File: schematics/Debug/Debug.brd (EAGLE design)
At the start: 100 x 80 mm, 12 parts

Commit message: Debug plata
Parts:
- removed JP1: (no value), pinhead:1X06
- removed JP2, JP3, JP5, JP6, JP7, JP8: (no value), pinhead:1X02
- removed JP9: (no value), pinhead:1X03
- added BUS0, BUS1, RADIO_M1, RESET, U_ESP32, U_STM32: (no value), pinhead:1X02
- added GND: (no value), pinhead:1X06
- added SWD/UART: (no value), pinhead:1X03
- R1, R2: device resistor:0204/5 -> rcl:R0603
- moved S1 57.9 mm to (17.5, 16.2), turned to 270 degrees
- moved R1 51.9 mm to (6.08, 31.6), turned to 270 degrees
- moved R2 49.4 mm to (3.08, 31.6), turned to 270 degrees
- moved U$1 46.6 mm to (19.9, 39.2)
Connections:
- removed net N$1: JP5.2, U$1.TX1
- removed net N$10: JP1.1, JP1.2, JP1.3, JP1.4, JP1.5, JP1.6, JP3.1, JP6.2, JP8.1, JP9.3, S1.3, S1.4, U$1.GND0, U$1.GND1
- removed net N$11: JP9.2, U$1.SWDIO
- removed net N$12: JP9.1, U$1.SWDCLK
- removed net N$2: JP5.1, U$1.RX1
- removed net N$3: JP7.1, U$1.RX0
- removed net N$4: JP8.2, S1.1, S1.2, U$1.P$6
- removed net N$5: JP7.2, U$1.TX0
- removed net N$6: JP3.2, JP6.1, R2.2, U$1.VBUS0, U$1.VBUS1
- removed net N$9: JP2.2, U$1.M1
- new net BUS: BUS0.1, BUS1.2, R2.2, U$1.BUS0, U$1.BUS1
- new net GND: BUS0.2, BUS1.1, GND.1, GND.2, GND.3, GND.4, GND.5, GND.6, RESET.1, S1.3, S1.4, SWD/UART.3, U$1.GND0, U$1.GND1
- new net M1: RADIO_M1.2, U$1.M1
- new net RESET: RESET.2, S1.1, S1.2, U$1.RESET
- new net RX+: U$1.RX1, U_ESP32.1
- new net RX-: U$1.RX0, U_STM32.1
- new net SWC: SWD/UART.1, U$1.SWC
- new net SWD: SWD/UART.2, U$1.SWD
- new net TX+: U$1.TX1, U_ESP32.2
- new net TX-: U$1.TX0, U_STM32.2
- net N$7: now also RADIO_M1.1; no longer JP2.1
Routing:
- net GND: track 0.00 -> 117.0 mm
- net N$10: track 87.3 -> 0.00 mm
- net BUS: track 0.00 -> 83.8 mm, vias 0 -> 1
- net TX-: track 0.00 -> 40.7 mm, vias 0 -> 2
- net SWC: track 0.00 -> 36.8 mm
- net RX+: track 0.00 -> 34.6 mm
- net TX+: track 0.00 -> 33.8 mm
- net RX-: track 0.00 -> 33.6 mm, vias 0 -> 1
- net RESET: track 0.00 -> 30.9 mm, vias 0 -> 1
- net SWD: track 0.00 -> 29.6 mm
- net N$9: track 24.6 -> 0.00 mm
- net M1: track 0.00 -> 21.9 mm, vias 0 -> 1
- net N$12: track 21.1 -> 0.00 mm
- net N$4: track 13.7 -> 0.00 mm
- net N$6: track 12.8 -> 0.00 mm
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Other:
- board size 100 x 80 mm -> 37.1 x 39.3 mm
- board text added: "BUS"
- board text added: "GND"
- board text added: "RX"
- board text added: "SWC/TX"
- board text added: "SWD/RX"
- board text added: "TX"
- board text added: "Замкнуть для конфигурации радио"

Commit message: Очередная дебажная плата
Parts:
- removed BUS0, U_ESP32, U_STM32: (no value), pinhead:1X02
- removed GND: (no value), pinhead:1X06
- removed SWD/UART: (no value), pinhead:1X03
- added BUS2, BUS3, BUS4, DB_ESP, DB_STM, IO0, RESET1: (no value), pinhead:1X02
- added DL_ESP, DL_STM: (no value), pinhead:1X03
- added GND1: (no value), pinhead:1X06
- added S2, S3: (no value), switch-omron:B3F-10XX
- added U$2: USB-C, CanCubeSat:USB-C
- moved BUS1 37.8 mm to (33.9, 41.6), turned to 180 degrees
- moved RADIO_M1 19.5 mm to (24.0, 27.6), turned to 90 degrees
- moved R2 15.0 mm to (17.0, 26.0), turned to 0 degrees
- moved R1 11.2 mm to (17.0, 29.0), turned to 0 degrees
- moved RESET 10.5 mm to (20.9, 9.09), turned to 180 degrees
- moved U$1 5.81 mm to (20.0, 45.0)
- moved S1 3.91 mm to (20.9, 18.1), turned to 0 degrees
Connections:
- removed net RX+: U$1.RX1, U_ESP32.1
- removed net RX-: U$1.RX0, U_STM32.1
- removed net SWC: SWD/UART.1, U$1.SWC
- removed net SWD: SWD/UART.2, U$1.SWD
- removed net TX+: U$1.TX1, U_ESP32.2
- removed net TX-: U$1.TX0, U_STM32.2
- new net 3V3: BUS2.2, BUS3.2, U$1.SWC, U$2.SWC
- new net N$3: IO0.1, S3.3, S3.4, U$1.SWD
- new net RESET_STM: RESET1.2, S2.1, S2.2, U$2.RESET
- new net RX0: DB_ESP.1, U$1.RX0
- new net RX0_STM: DB_STM.1, U$2.RX0
- new net RX1: DL_ESP.2, U$1.RX1
- new net SWC_STM: DL_STM.3, U$2.TX1
- new net SWD_STM: DL_STM.2, U$2.RX1
- new net TX0: DB_ESP.2, U$1.TX0
- new net TX0_STM: DB_STM.2, U$2.TX0
- new net TX1: DL_ESP.3, U$1.TX1
- net BUS: now also BUS4.2, U$2.BUS0, U$2.BUS1; no longer BUS0.1
- net GND: now also BUS2.1, BUS3.1, BUS4.1, DL_STM.1, GND1.1, GND1.2, GND1.3, GND1.4, GND1.5, GND1.6, IO0.2, RESET1.1, S2.3, S2.4, S3.1, S3.2, U$2.GND0, U$2.GND1; no longer BUS0.2, GND.1, GND.2, GND.3, GND.4, GND.5, GND.6, SWD/UART.3
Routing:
- net GND: track 117.0 -> 187.2 mm, vias 0 -> 1
- net N$3: track 0.00 -> 49.2 mm, vias 0 -> 1
- net 3V3: track 0.00 -> 49.0 mm, vias 0 -> 1
- net BUS: track 83.8 -> 127.4 mm
- net TX-: track 40.7 -> 0.00 mm, vias 2 -> 0
- net RESET_STM: track 0.00 -> 37.1 mm, vias 0 -> 1
- net SWC: track 36.8 -> 0.00 mm
- net RX+: track 34.6 -> 0.00 mm
- net TX+: track 33.8 -> 0.00 mm
- net RX-: track 33.6 -> 0.00 mm, vias 1 -> 0
- net SWD: track 29.6 -> 0.00 mm
- net TX0: track 0.00 -> 29.5 mm, vias 0 -> 1
- net RX0: track 0.00 -> 24.5 mm
- net TX1: track 0.00 -> 17.0 mm
- net RX1: track 0.00 -> 16.4 mm
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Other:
- board size 37.1 x 39.3 mm -> 63.8 x 42.5 mm
- board text removed: "BUS"
- board text removed: "GND"
- board text removed: "RX"
- board text removed: "SWC/TX"
- board text removed: "SWD/RX"
- board text removed: "TX"

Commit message: Отладочная плата v2
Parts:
- removed BUS1, BUS2, BUS3, BUS4, DB_ESP, DB_STM, RADIO_M1, RESET, RESET1: (no value), pinhead:1X02
- removed DL_ESP, DL_STM: (no value), pinhead:1X03
- removed GND1: (no value), pinhead:1X06
- removed R1: 1k, rcl:R0603
- removed R2: 10k, rcl:R0603
- removed S1, S2, S3: (no value), switch-omron:B3F-10XX
- added C1, C2, C3: 1nF, rcl:C0603
- added DEBUG_STM32: (no value), pinhead:1X03
- added DOWNLOAD_ESP32: (no value), pinhead:1X05
- added DOWNLOAD_STM32, RADIO: (no value), pinhead:1X04
- added EN, NRST: (no value), switch-omron:B3F-10XX
- added ENABLE, GPIO0, JP1, JP5, JP6, JP7, JP8, NRESET: (no value), pinhead:1X02
- added JP2: (no value), pinhead:1X06
- IO0: device pinhead:1X02 -> switch-omron:B3F-10XX
- moved IO0 39.9 mm to (36.0, 49.0), turned to 90 degrees
- moved U$1 32.0 mm to (21.1, 77.0)
- moved U$2 32.0 mm to (55.1, 77.0)
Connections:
- removed net N$3: IO0.1, S3.3, S3.4, U$1.SWD
- removed net N$7: R1.2, RADIO_M1.1
- removed net N$8: R1.1, R2.1
- removed net RESET: RESET.2, S1.1, S1.2, U$1.RESET
- removed net RESET_STM: RESET1.2, S2.1, S2.2, U$2.RESET
- removed net RX0: DB_ESP.1, U$1.RX0
- removed net RX0_STM: DB_STM.1, U$2.RX0
- removed net SWC_STM: DL_STM.3, U$2.TX1
- removed net SWD_STM: DL_STM.2, U$2.RX1
- removed net TX0: DB_ESP.2, U$1.TX0
- removed net TX0_STM: DB_STM.2, U$2.TX0
- new net 3V3-S: JP1.1, U$1.NC/3V3
- new net EN: C2.2, DOWNLOAD_ESP32.5, EN.3, EN.4, ENABLE.2, U$1.NRST/EN
- new net IO0: C1.2, DOWNLOAD_ESP32.4, GPIO0.2, IO0.3, IO0.4, U$1.NC/GPIO
- new net NRST: C3.2, DOWNLOAD_STM32.4, NRESET.2, NRST.3, NRST.4, U$2.NRST/EN
- new net RX: DEBUG_STM32.3, U$2.RX0
- new net RXD: DOWNLOAD_ESP32.3, U$1.SWD/RXD
- new net SWC: DOWNLOAD_STM32.2, U$2.SWC/TXD
- new net SWD: DOWNLOAD_STM32.3, U$2.SWD/RXD
- new net TX: DEBUG_STM32.2, U$2.TX0
- new net TXD: DOWNLOAD_ESP32.2, U$1.SWC/TXD
- net 3V3: now also JP5.2, JP7.2, U$2.NC/3V3; no longer BUS2.2, BUS3.2, U$1.SWC, U$2.SWC
- net BUS: now also JP6.2, JP8.2, U$1.3V3/BUS0, U$1.3V3/BUS1, U$2.3V3/BUS0, U$2.3V3/BUS1; no longer BUS1.2, BUS4.2, R2.2, U$1.BUS0, U$1.BUS1, U$2.BUS0, U$2.BUS1
- net GND: now also C1.1, C2.1, C3.1, DEBUG_STM32.1, DOWNLOAD_ESP32.1, DOWNLOAD_STM32.1, EN.1, EN.2, ENABLE.1, GPIO0.1, IO0.1, JP2.1, JP2.2, JP2.3, JP2.4, JP2.5, JP2.6, JP5.1, JP6.1, JP7.1, JP8.1, NRESET.1, NRST.1, NRST.2, RADIO.1; no longer BUS1.1, BUS2.1, BUS3.1, BUS4.1, DL_STM.1, GND1.1, GND1.2, GND1.3, GND1.4, GND1.5, GND1.6, RESET.1, RESET1.1, S1.3, S1.4, S2.3, S2.4, S3.1, S3.2
- net M1: now also JP1.2, RADIO.4, U$1.NC/M1; no longer RADIO_M1.2, U$1.M1
- net RX1: now also RADIO.3, U$1.RX0; no longer DL_ESP.2, U$1.RX1
- net TX1: now also RADIO.2, U$1.TX0; no longer DL_ESP.3, U$1.TX1
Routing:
- net EN: track 0.00 -> 91.6 mm, vias 0 -> 1
- net IO0: track 0.00 -> 84.9 mm, vias 0 -> 1
- net GND: track 187.2 -> 252.2 mm
- net NRST: track 0.00 -> 62.0 mm
- net RX: track 0.00 -> 52.5 mm, vias 0 -> 1
- net N$3: track 49.2 -> 0.00 mm, vias 1 -> 0
- net TX: track 0.00 -> 46.0 mm, vias 0 -> 1
- net SWC: track 0.00 -> 45.4 mm, vias 0 -> 1
- net M1: track 10.4 -> 53.2 mm
- net RESET: track 40.2 -> 0.00 mm, vias 1 -> 0
- net SWD: track 0.00 -> 38.3 mm, vias 0 -> 1
- net RESET_STM: track 37.1 -> 0.00 mm, vias 1 -> 0
- net RXD: track 0.00 -> 36.3 mm
- net TXD: track 0.00 -> 36.0 mm
- net TX1: track 17.0 -> 48.5 mm, vias 0 -> 2
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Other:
- board size 63.8 x 42.5 mm -> 79.4 x 53.3 mm
- board text removed: "Замкнуть для конфигурации радио"

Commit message: Отладочная плата v3
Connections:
- net 3V3: now also U$2.3V3/BUS0, U$2.3V3/BUS1; no longer U$2.NC/3V3
- net BUS: no longer U$2.3V3/BUS0, U$2.3V3/BUS1
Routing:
- net BUS: track 115.0 -> 77.2 mm
- net GND: track 252.2 -> 267.8 mm, vias 1 -> 3
- net IO0: track 84.9 -> 69.6 mm, vias 1 -> 2
- net RX: track 52.5 -> 39.0 mm
- net EN: track 91.6 -> 79.5 mm, vias 1 -> 0
- net 3V3-S: track 31.3 -> 20.1 mm
- net NRST: track 62.0 -> 72.3 mm
- net RX1: track 45.6 -> 55.1 mm, vias 1 -> 0
- net 3V3: track 29.2 -> 37.4 mm
- net SWC: track 45.4 -> 37.3 mm
- net TX1: track 48.5 -> 40.8 mm, vias 2 -> 0
- net TX: track 46.0 -> 38.5 mm, vias 1 -> 0
- net M1: track 53.2 -> 46.4 mm
- net RXD: track 36.3 -> 35.6 mm

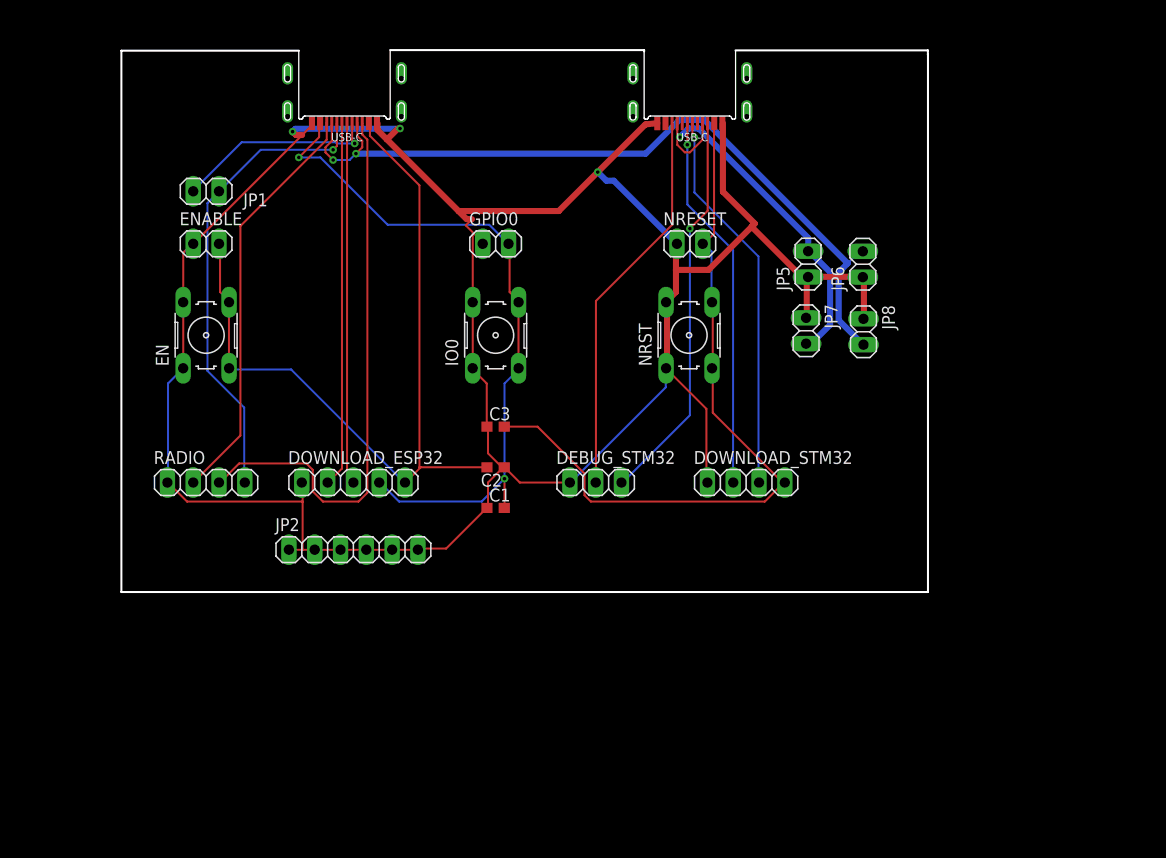
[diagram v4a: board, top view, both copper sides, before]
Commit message: Логическая схема для сбросом и управление бутлоадером ESP32 на отладочной плате.
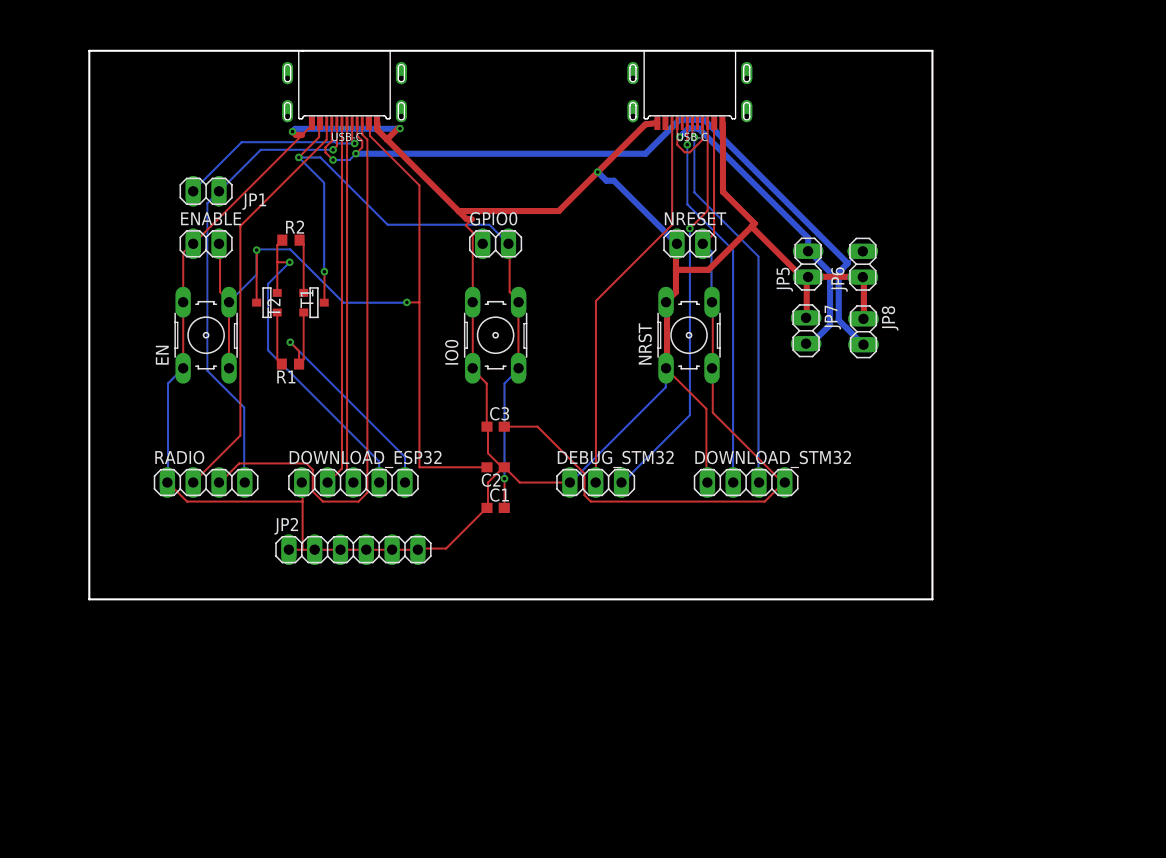
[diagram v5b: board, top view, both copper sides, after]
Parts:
- added R1, R2: 10, rcl:R0603
- added T1, T2: 2n7002, zetex:SOT-23
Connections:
- new net DTR: DOWNLOAD_ESP32.5, R1.1, T2.2
- new net N$1: R2.2, T2.3
- new net N$2: R1.2, T1.3
- new net RTS: DOWNLOAD_ESP32.4, R2.1, T1.2
- net EN: now also T1.1; no longer DOWNLOAD_ESP32.5
- net IO0: now also T2.1; no longer DOWNLOAD_ESP32.4
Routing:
- net RTS: track 0.00 -> 33.7 mm, vias 0 -> 1
- net DTR: track 0.00 -> 26.3 mm, vias 0 -> 1
- net EN: track 79.5 -> 85.1 mm, vias 0 -> 2
- net N$1: track 0.00 -> 5.36 mm
- net N$2: track 0.00 -> 5.26 mm
- net IO0: track 69.6 -> 70.9 mm, vias 2 -> 3
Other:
- board size 79.4 x 53.3 mm -> 83 x 54 mm

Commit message: Внёс незначительные правки на платах. Но пока не везде
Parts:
- added 3V3, 8V: (no value), led:CHIPLED_0603
- added R3, R4: 2k, rcl:R0603
- moved JP5 10.2 mm to (69.0, 46.0)
- moved JP7 8.20 mm to (74.0, 46.0), turned to 90 degrees
- moved JP8 4.99 mm to (74.0, 54.0), turned to 90 degrees
- moved JP6 3.73 mm to (69.0, 54.0)
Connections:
- new net N$3: 3V3.C, R4.2
- new net N$4: 8V.C, R3.2
- net 3V3: now also 3V3.A
- net BUS: now also 8V.A
- net GND: now also R3.1, R4.1
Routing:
- net GND: track 267.9 -> 298.6 mm
- net 3V3: track 37.5 -> 49.5 mm
- net IO0: track 70.9 -> 67.6 mm
- net N$4: track 0.00 -> 2.64 mm
- net N$3: track 0.00 -> 2.64 mm
- net NRST: track 72.3 -> 73.8 mm
- net RX1: track 55.1 -> 56.6 mm
- net BUS: track 77.2 -> 75.8 mm
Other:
- outline, holes or cut-outs redrawn

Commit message: Подписал контакты, отправил плату в производство
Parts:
- removed 3V3, 8V: (no value), led:CHIPLED_0603
- added LED1, LED2: (no value), led:CHIPLED_0603
- moved JP2 28.4 mm to (39.0, 5.09)
- moved R3 23.3 mm to (68.0, 29.7)
- moved R4 23.3 mm to (68.0, 21.7)
- moved C1 23.3 mm to (40.0, 9.00)
- moved C2 23.3 mm to (40.0, 13.0)
- moved C3 23.3 mm to (40.0, 17.0)
- moved DEBUG_STM32 23.3 mm to (49.9, 11.5)
- moved DOWNLOAD_ESP32 23.3 mm to (26.0, 11.5)
- moved DOWNLOAD_STM32 23.3 mm to (64.7, 11.5)
- moved EN 23.3 mm to (11.5, 26.0)
- moved ENABLE 23.3 mm to (11.5, 35.0)
- moved GPIO0 23.3 mm to (40.0, 35.0)
- moved IO0 23.3 mm to (40.0, 26.0)
- moved JP1 23.3 mm to (11.5, 40.2)
- moved JP5 23.3 mm to (73.0, 23.0)
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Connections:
- net 3V3: now also LED1.A; no longer 3V3.A
- net BUS: now also LED2.A; no longer 8V.A
- net N$3: now also LED1.C; no longer 3V3.C
- net N$4: now also LED2.C; no longer 8V.C
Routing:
- net GND: track 298.6 -> 286.8 mm
- net 3V3: track 49.5 -> 48.0 mm
- net 3V3-S: track 20.2 -> 21.1 mm
- added copper zone on layer 1, net GND
- added copper zone on layer 16, net GND
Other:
- board size 83 x 54 mm -> 84 x 54 mm
- board text added: "3V3"
- board text added: "BUS+"
- board text added: "DEBUG STM32"
- board text added: "DOWNLOAD ESP32"
- board text added: "DOWNLOAD STM32"
- board text added: "DTR"
- board text added: "ESP32 EN (LOW)"
- board text added: "ESP32 GPIO0 (LOW)"
- board text added: "GND"
- board text added: "M1"
- board text added: "NRST"
- board text added: "PWR 3V3"
- board text added: "PWR BUS (8V)"
- board text added: "RADIO"
- board text added: "RADIO M1 (HIGH)"
- board text added: "RTS"
- board text added: "RX"
- board text added: "RX1"
- board text added: "RXD"
- board text added: "STM32 NRST (LOW)"
- board text added: "SWC"
- board text added: "SWD"
- board text added: "TX"
- board text added: "TX1"
- board text added: "TXD"
- board text added: "USB-C to ESP32"
- board text added: "USB-C to STM32"
